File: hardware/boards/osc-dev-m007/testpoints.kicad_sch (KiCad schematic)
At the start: 29 parts, among them J1201 Conn_01x06, J1202 Conn_01x06

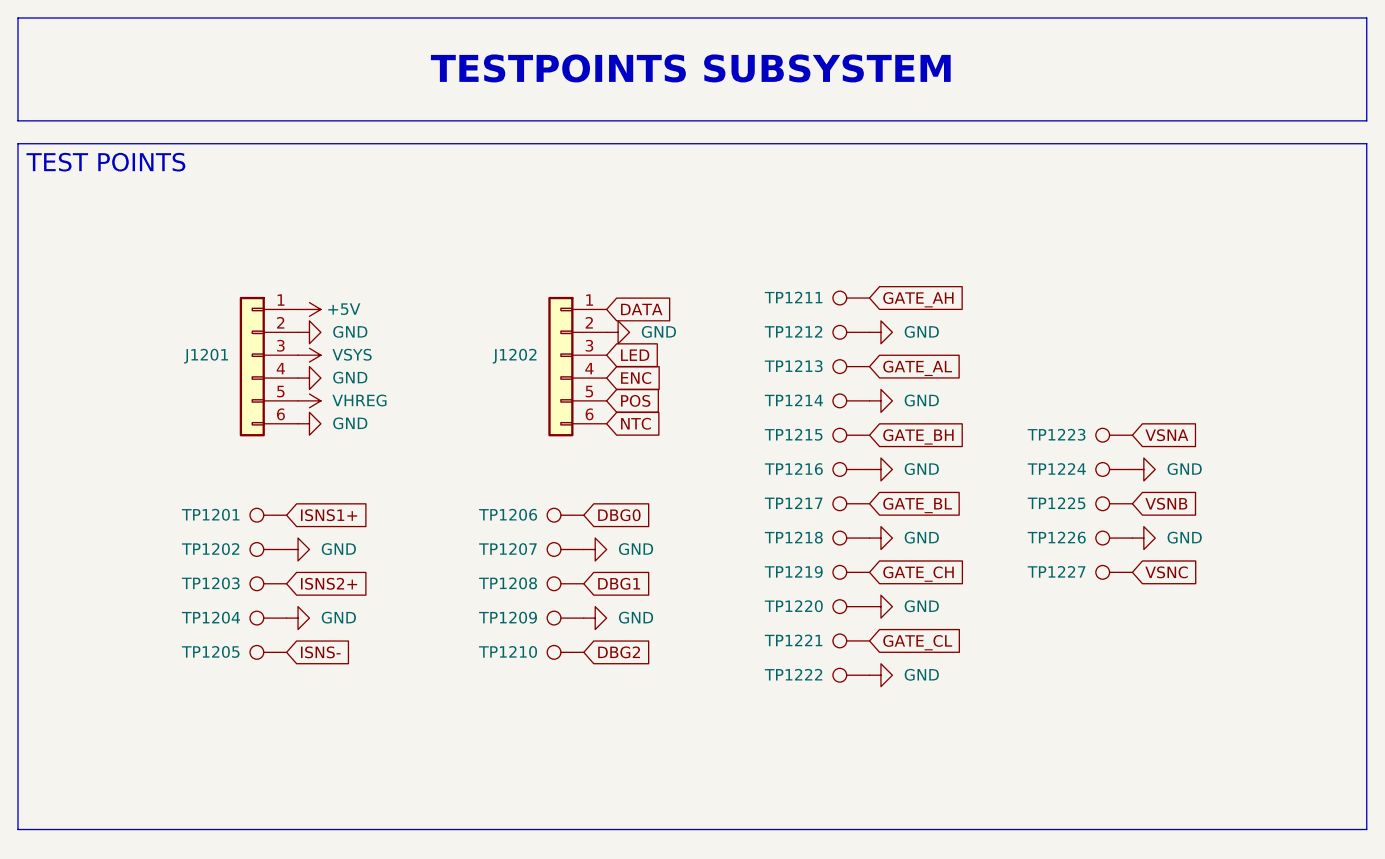
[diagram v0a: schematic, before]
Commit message: hw: design osc-dev-m007 pcb
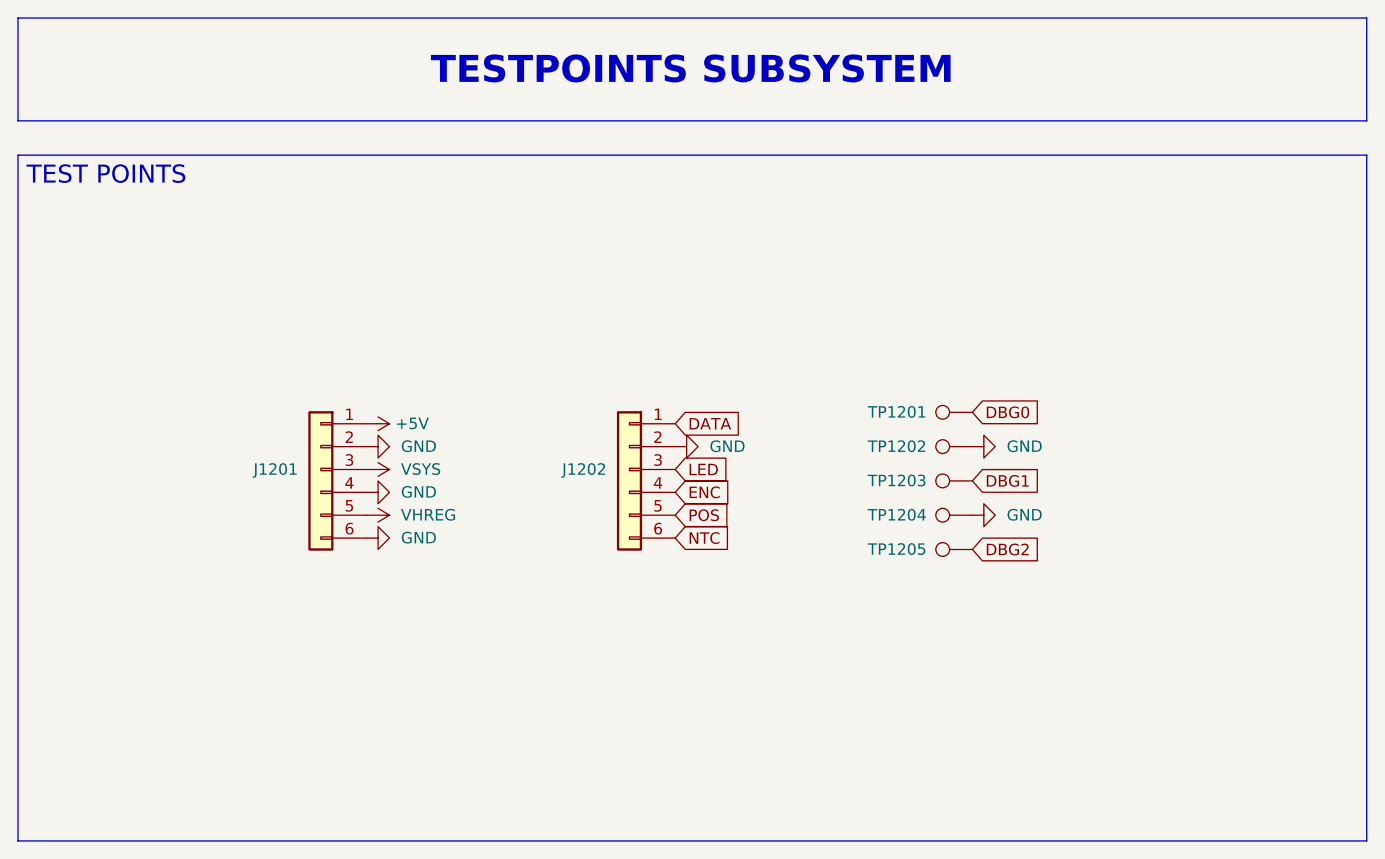
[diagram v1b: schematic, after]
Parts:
- removed TP1201, TP1202, TP1203, TP1204, TP1205, TP1211, TP1212, TP1213, TP1214, TP1215, TP1216, TP1217, TP1218, TP1219, TP1220, TP1221, TP1222, TP1223, TP1224, TP1225, TP1226, TP1227: TestPoint, symbol Connector:TestPoint
- J1201, J1202: footprint (none) -> Connector_PinHeader_2.54mm:PinHeader_1x06_P2.54mm_Vertical
- TP1201: renamed from TP1206; footprint (none) -> TestPoint:TestPoint_Pad_D1.0mm
- TP1202: renamed from TP1207; footprint (none) -> TestPoint:TestPoint_Pad_D1.0mm
- TP1203: renamed from TP1208; footprint (none) -> TestPoint:TestPoint_Pad_D1.0mm
- TP1204: renamed from TP1209; footprint (none) -> TestPoint:TestPoint_Pad_D1.0mm
- TP1205: renamed from TP1210; footprint (none) -> TestPoint:TestPoint_Pad_D1.0mm
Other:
- moved on the sheet: J1201, J1202, TP1201, TP1202, TP1203, TP1204, TP1205

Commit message: hw: swap dev-m007 parts to in-stock equivalents
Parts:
- added TP1206: TestPoint, TestPoint:TestPoint_Pad_D1.0mm, symbol Connector:TestPoint
- J1201, J1202, TP1201, TP1202, TP1203, TP1204, TP1205: now left out of the parts list
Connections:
- net GND: now also TP1206.1
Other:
- note added: "Place near ISNS nodes"
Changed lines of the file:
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@@
 	(generator_version "10.0")
 	(paper "A4")
+	(text "Place near ISNS nodes"
+		(exclude_from_sim no)
+		(at 87.63 92.964 0)
+		(effects
+			(font
+				(size 1.27 1.27)
+			)
+		)
+	)
 	(text_box "TEST POINTS"
 		(exclude_from_sim no)
@@
 		(body_style 1)
 		(exclude_from_sim no)
-		(in_bom yes)
+		(in_bom no)
 		(on_board yes)
 		(in_pos_files yes)
@@
 		(body_style 1)
 		(exclude_from_sim no)
-		(in_bom yes)
+		(in_bom no)
 		(on_board yes)
 		(in_pos_files yes)
@@
 		(body_style 1)
 		(exclude_from_sim no)
-		(in_bom yes)
+		(in_bom no)
 		(on_board yes)
 		(in_pos_files yes)
@@
 		(body_style 1)
 		(exclude_from_sim no)
-		(in_bom yes)
+		(in_bom no)
 		(on_board yes)
 		(in_pos_files yes)
@@
 	(symbol
 		(lib_id "power:GND")
+		(at 90.17 88.9 90)
+		(unit 1)
+		(body_style 1)
+		(exclude_from_sim no)
+		(in_bom yes)
+		(on_board yes)
+		(in_pos_files yes)
+		(dnp no)
+		(fields_autoplaced yes)
+		(property "Reference" "#PWR01210"
+			(at 96.52 88.9 0)
+			(hide yes)
+			(show_name no)
+			(do_not_autoplace no)
+			(effects
+				(font
+					(size 1.27 1.27)
+				)
+			)
+		)
+		(property "Value" "GND"
+			(at 93.98 88.8999 90)
+			(show_name no)
+			(do_not_autoplace no)
+			(effects
+				(font
+					(size 1.27 1.27)
+				)
+				(justify right)
+			)
+		)
+		(property "Footprint" ""
+			(at 90.17 88.9 0)
+			(hide yes)
+			(show_name no)
+			(do_not_autoplace no)
+			(effects
+				(font
+					(size 1.27 1.27)
+				)
+			)
+		)
+		(property "Datasheet" ""
+			(at 90.17 88.9 0)
+			(hide yes)
+			(show_name no)
+			(do_not_autoplace no)
+			(effects
+				(font
+					(size 1.27 1.27)
+				)
+			)
+		)
+		(property "Description" "Power symbol creates a global label with name \"GND\" , ground"
+			(at 90.17 88.9 0)
+			(hide yes)
+			(show_name no)
+			(do_not_autoplace no)
+			(effects
+				(font
+					(size 1.27 1.27)
+				)
+			)
+		)
+		(pin "1"
+		)
+		(instances
+			(project "osc-dev-m007"
+				(path "/6062e7d2-0c72-467e-b49c-6387ba053e09/4047ca50-6cee-462e-8aea-0fd4ac81b1ba"
+					(reference "#PWR01210")
+					(unit 1)
+				)
+			)
+		)
+	)
+	(symbol
+		(lib_id "Connector:TestPoint")
+		(at 90.17 88.9 90)
+		(unit 1)
+		(body_style 1)
+		(exclude_from_sim no)
+		(in_bom no)
+		(on_board yes)
+		(in_pos_files yes)
+		(dnp no)
+		(property "Reference" "TP1206"
+			(at 85.09 88.9 90)
+			(show_name no)
+			(do_not_autoplace no)
+			(effects
+				(font
+					(size 1.27 1.27)
+				)
+				(justify left)
+			)
+		)
+		(property "Value" "TestPoint"
+			(at 86.868 85.725 90)
+			(hide yes)
+			(show_name no)
+			(do_not_autoplace no)
+			(effects
+				(font
+					(size 1.27 1.27)
+				)
+			)
+		)
+		(property "Footprint" "TestPoint:TestPoint_Pad_D1.0mm"
+			(at 90.17 83.82 0)
+			(hide yes)
+			(show_name no)
+			(do_not_autoplace no)
+			(effects
+				(font
+					(size 1.27 1.27)
+				)
+			)
+		)
+		(property "Datasheet" ""
+			(at 90.17 83.82 0)
+			(hide yes)
+			(show_name no)
+			(do_not_autoplace no)
+			(effects
+				(font
+					(size 1.27 1.27)
+				)
+			)
+		)
+		(property "Description" "test point"
+			(at 90.17 88.9 0)
+			(hide yes)
+			(show_name no)
+			(do_not_autoplace no)
+			(effects
+				(font
+					(size 1.27 1.27)
+				)
+			)
+		)
+		(pin "1"
+		)
+		(instances
+			(project "osc-dev-m007"
+				(path "/6062e7d2-0c72-467e-b49c-6387ba053e09/4047ca50-6cee-462e-8aea-0fd4ac81b1ba"
+					(reference "TP1206")
+					(unit 1)
+				)
+			)
+		)
+	)
+	(symbol
+		(lib_id "power:GND")
 		(at 53.34 72.39 90)
 		(unit 1)
@@
 		(body_style 1)
 		(exclude_from_sim no)
-		(in_bom yes)
+		(in_bom no)
 		(on_board yes)
 		(in_pos_files yes)
@@
 		(body_style 1)
 		(exclude_from_sim no)
-		(in_bom yes)
+		(in_bom no)
 		(on_board yes)
 		(in_pos_files yes)
@@
 		(body_style 1)
 		(exclude_from_sim no)
-		(in_bom yes)
-		(on_board yes)
-		(in_pos_files yes)
+		(in_bom no)
+		(on_board yes)
+		(in_pos_files yes)
